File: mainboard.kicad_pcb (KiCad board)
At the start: 2 copper layers, 80 x 110 mm, 33 parts, among them J1 terminal_led-strip, J2 header_rotary-encoder, J4 header_pi, J5 power_input, J6 AudioJack2, Q1 IRF9540N, SW1 power_switch, U1 OPA2277, U2 MSGEQ7, U4 logic-level-converter, U5 logic-level-converter

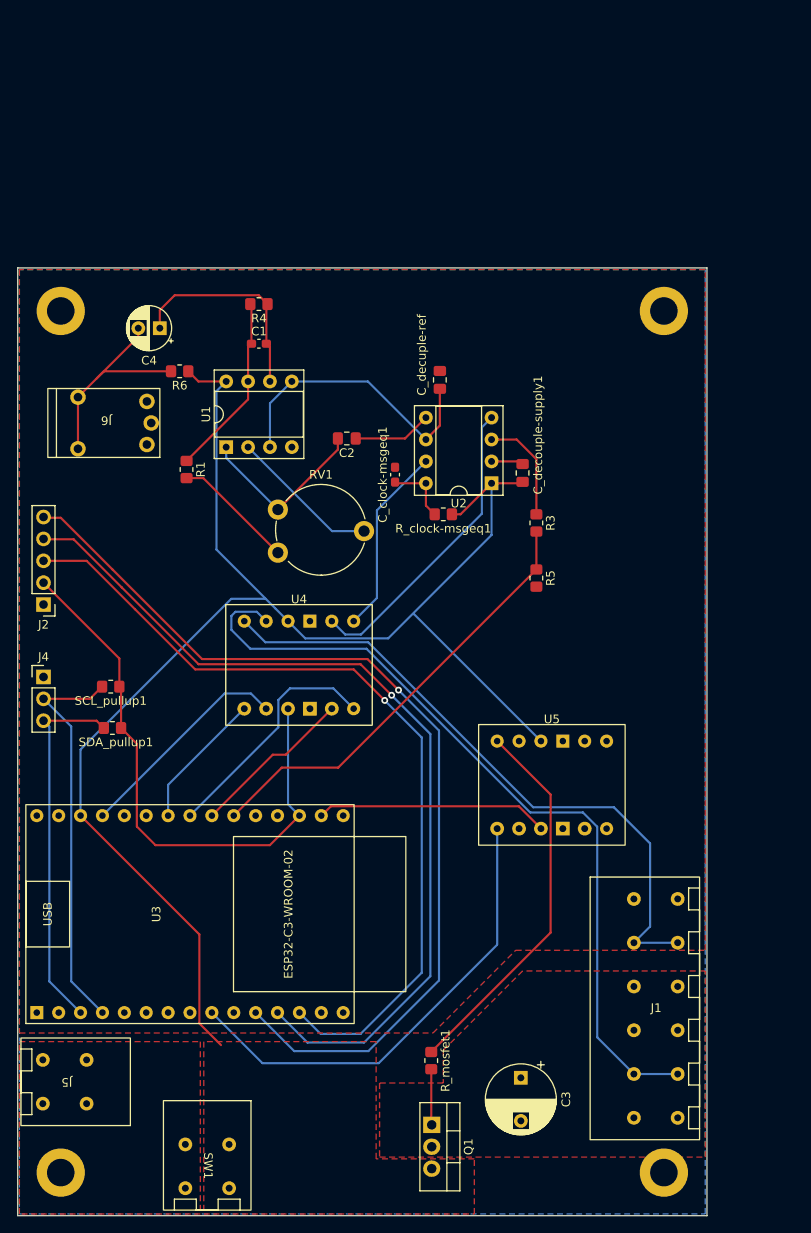
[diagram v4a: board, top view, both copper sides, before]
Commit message: ground mounting holes
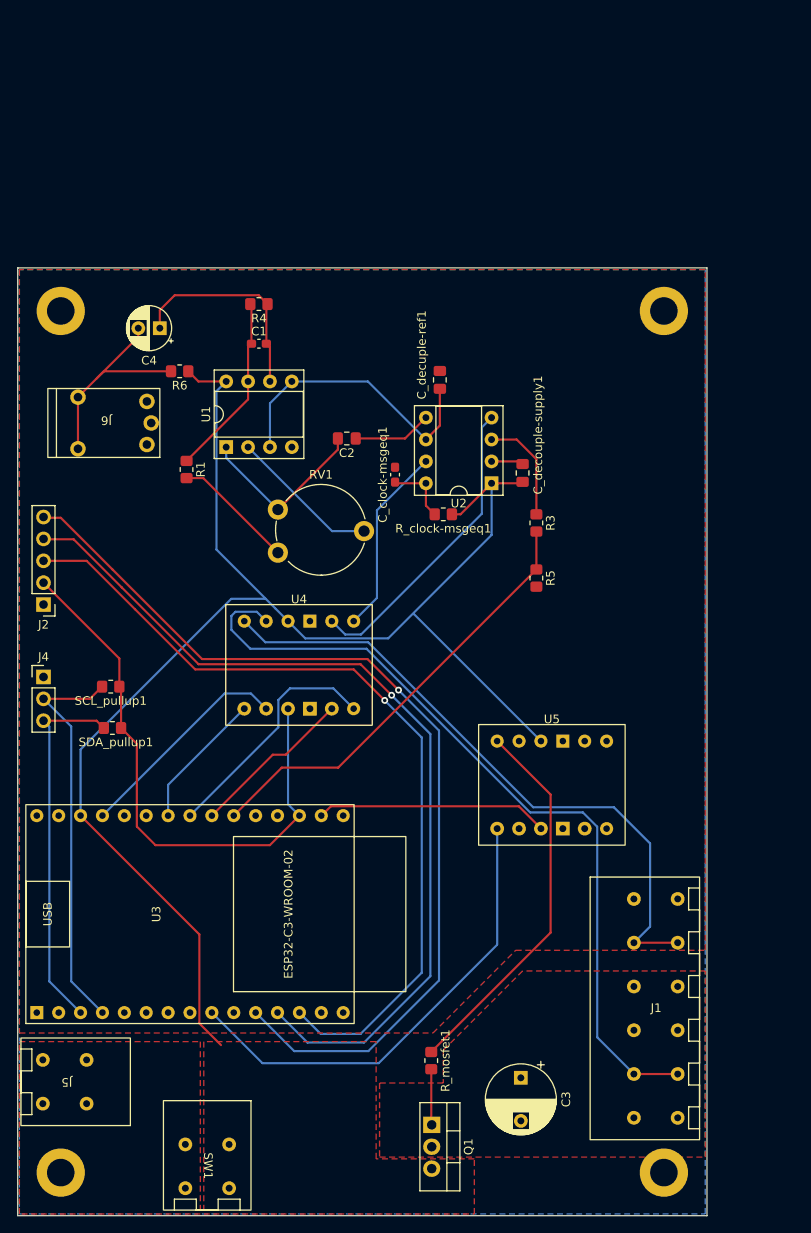
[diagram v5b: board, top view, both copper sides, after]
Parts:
- renumbered C_decuple-ref to C_decuple-ref1
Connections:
- REF** pad 1: (no net) -> GND (x4)
